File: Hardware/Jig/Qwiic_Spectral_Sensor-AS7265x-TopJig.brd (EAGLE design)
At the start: 35.6 x 40.6 mm, 93 parts, among them J2 Serial Interface, J5 Flash Programming, J8 PTH, U1 AS72651, U3 4MB Flash, U5 AS72653, U6 AS72652

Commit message: Silk changes before panelization
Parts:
- removed U$1, U$36, U$37: (no value), buzzard_labels (7):#0
- removed U$38, U$39, U$40: (no value), buzzard_labels (7):#1
- added E$1, E$2, E$3, E$4: (no value), SparkFun-Hardware:STAND-OFF-TIGHT
- added E$5, E$6: (no value), SparkFun-Hardware:NUBBIN_LOCKER
- D2: device SparkFun-LED:SUPER_BRIGHT_SMD_LED_3014 -> SparkX:SUPER_BRIGHT_SMD_LED_1206
- moved U$6 0.25 mm to (28.1, 21.3)
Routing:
- net 3.3V: track 143.3 -> 0.00 mm, vias 4 -> 0
- net RX/SCL: track 99.0 -> 0.00 mm, vias 6 -> 0
- net TX/SDA: track 93.2 -> 0.00 mm, vias 5 -> 0
- net SDA_S: track 56.9 -> 0.00 mm, vias 3 -> 0
- net SCL_S: track 56.2 -> 0.00 mm, vias 3 -> 0
- net !RST: track 50.8 -> 0.00 mm, vias 3 -> 0
- net !INT: track 30.2 -> 0.00 mm, vias 1 -> 0
- net LED_DRV: track 21.0 -> 0.00 mm, vias 1 -> 0
- net !CS_EE: track 17.6 -> 0.00 mm, vias 2 -> 0
- net I2C_ENB: track 16.8 -> 0.00 mm, vias 1 -> 0
- net MISO: track 15.5 -> 0.00 mm, vias 1 -> 0
- net !RST-ADDR: track 14.9 -> 0.00 mm, vias 2 -> 0
- net N$2: track 11.8 -> 0.00 mm, vias 2 -> 0
- net MOSI: track 9.65 -> 0.00 mm
- net LED_DRV1: track 9.51 -> 0.00 mm
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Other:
- board size 35.6 x 40.6 mm -> 48.3 x 53.3 mm
- board text added: "#6"
- board text added: "6"
- board text added: "DEV-Me"
- board text added: "GPS-Test"

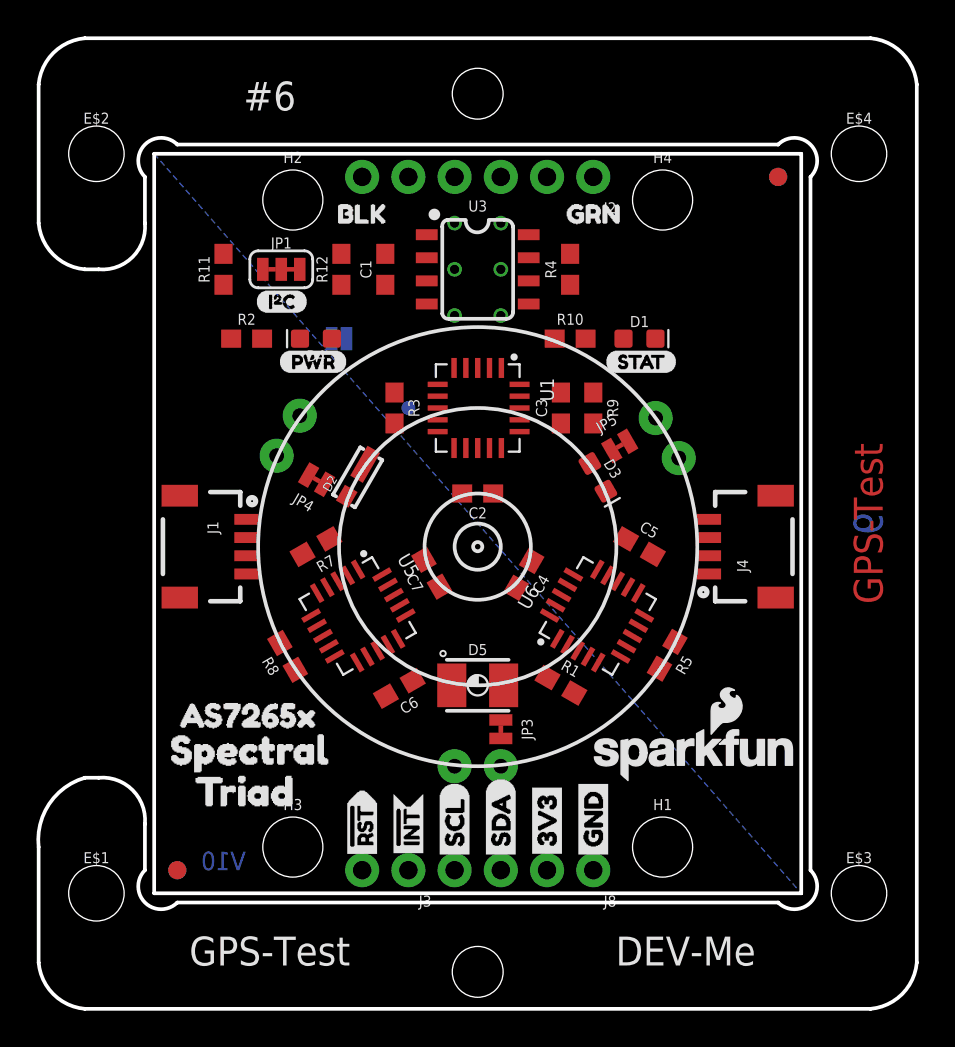
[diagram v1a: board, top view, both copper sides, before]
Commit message: Intermediate committ. Probably ignore the jig files.
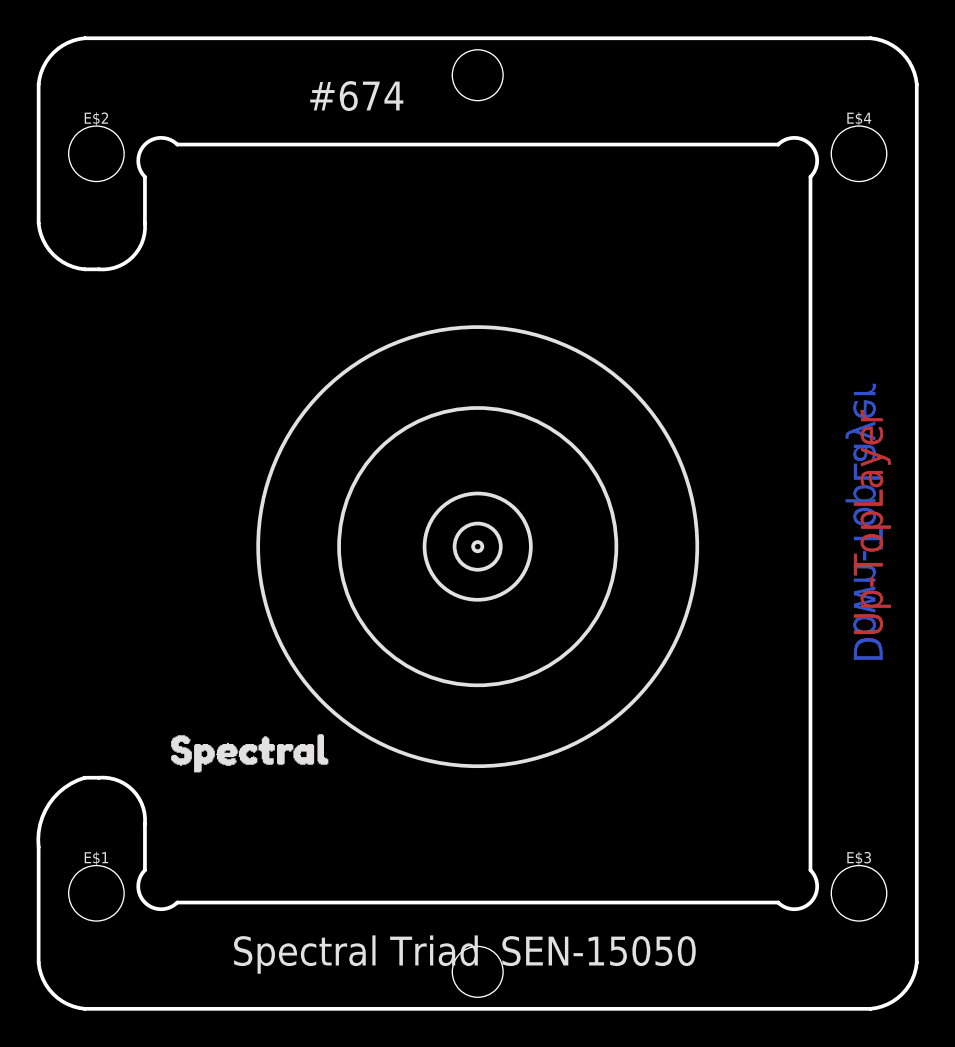
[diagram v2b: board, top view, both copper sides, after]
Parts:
- removed BULB1, BULB2, BULB3: (no value), SparkX:LED_5MM_NOSILK
- removed C1: 1.0uF, SparkFun-Capacitors:0603
- removed C2, C4, C6: 0.1uF, SparkFun-Capacitors:0603
- removed C3, C5, C7: 10uF, SparkFun-Capacitors:0603
- removed D1: BLUE, SparkFun-LED:LED-0603
- removed D2: 5700k, SparkX:SUPER_BRIGHT_SMD_LED_1206
- removed D3: IR, SparkFun-LED:LED-0603
- removed D4: RED, SparkFun-LED:LED-0603
- removed D5: UV, SparkFun-LED:PLCC-2
- removed FD1, FD2, FD3, FD4: FIDUCIAL1X2, SparkFun-Aesthetics:FIDUCIAL-1X2
- removed H1, H2, H3, H4: STAND-OFF, SparkFun-Hardware:STAND-OFF
- removed J1, J4: (no value), SparkFun-Connectors:1X04_1MM_RA
- removed J2: Serial Interface, SparkFun-Connectors:1X06_NO_SILK
- removed J3: (no value), SparkFun-Connectors:1X02_NO_SILK
- removed J5: Flash Programming, SparkFun-Connectors:2X3_TEST_POINTS
- removed J8: PTH, SparkFun-Connectors:1X04_NO_SILK
- removed JP1: (no value), SparkFun-Jumpers:SMT-JUMPER_3_2-NC_TRACE_SILK
- removed JP2: (no value), SparkFun-Jumpers:SMT-JUMPER_2_NO_SILK
- removed JP3, JP4, JP5: (no value), SparkFun-Jumpers:SMT-JUMPER_2_NC_TRACE_NO-SILK
- removed LOGO1: SFE_LOGO_NAME_FLAME.1_INCH, SparkFun-Aesthetics:SFE_LOGO_NAME_FLAME_.1
- removed LOGO4: OSHW-LOGOS, SparkFun-Aesthetics:OSHW-LOGO-S
- removed R1, R3, R4, R5, R7, R8: 10k, SparkFun-Resistors:0603
- removed R10, R11, R12, R9: 2.2k, SparkFun-Resistors:0603
- removed R2: 1k, SparkFun-Resistors:0603
- removed TP1: (no value), SparkFun-Connectors:PAD.03X.03
- removed U$10: (no value), buzzard_labels (50):STAT4
- removed U$11, U$12: (no value), buzzard_labels (50):TRIAD2
- removed U$13: (no value), buzzard_labels (50):SPECTRAL1
- removed U$14, U$4: (no value), buzzard_labels (50):AS7265X0
- removed U$15: (no value), buzzard_labels (51):3V33
- removed U$16: (no value), buzzard_labels (51):BLK7
- removed U$17: (no value), buzzard_labels (51):GND5
- removed U$18: (no value), buzzard_labels (51):GRN6
- removed U$19, U$20: (no value), buzzard_labels (51):NC4
- removed U$2: (no value), Labels:I_SUPER2_C-()-03
- removed U$21: (no value), buzzard_labels (51):RXI2
- removed U$22: (no value), buzzard_labels (51):SERIAL0
- removed U$23: (no value), buzzard_labels (51):TXO1
- removed U$24, U$31: (no value), Labels:3V3-04
- removed U$25, U$30: (no value), Labels:GND-04
- removed U$26, U$32: (no value), Labels:SDA-[)
- removed U$27, U$33: (no value), Labels:SCL-[)
- removed U$28, U$34: (no value), Labels:INT#-[<-04
- removed U$29, U$35: (no value), Labels:RST#-[>-04
- removed U$3: (no value), Labels:PWR-()-03
- removed U$5: (no value), buzzard_labels (50):BULB15
- removed U$6: (no value), buzzard_labels (50):BULB26
- removed U$7: (no value), buzzard_labels (50):BULB37
- removed U$8: (no value), buzzard_labels (52):JP20
- removed U1: AS72651, Qwiic_Spectral_Sensor-AS7265x:LGA20
- removed U3: 4MB Flash, SparkFun-IC-Memory:SO08
- removed U5: AS72653, Qwiic_Spectral_Sensor-AS7265x:LGA20
- removed U6: AS72652, Qwiic_Spectral_Sensor-AS7265x:LGA20
- moved E$6 1.02 mm to (17.8, 45.0)
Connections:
- removed net !CS_EE: J5.5, U1.6, U3.1
- removed net !INT: J3.1, U1.9
- removed net !RST: J3.2, R4.1, U1.2, U5.2
- removed net !RST-ADDR: U1.13, U6.2
- removed net 3.3V: BULB1.A, BULB2.A, BULB3.A, C1.1, C2.1, C3.1, C4.1, C5.1, C6.1, C7.1, D1.A, D4.A, J1.2, J2.4, J4.2, J5.2, J8.2, JP1.2, JP3.2, JP4.2, JP5.2, R10.2, R3.2, R4.2, R9.2, U1.14, U1.17, U3.3, U3.7, U3.8, U5.14, U5.17, U6.14, U6.17
- removed net GND: C1.2, C2.2, C3.2, C4.2, C5.2, C6.2, C7.2, J1.1, J2.6, J4.1, J5.6, J8.1, JP2.1, R1.1, R2.1, R5.1, R7.1, R8.1, U1.16, U3.4, U5.16, U6.16
- removed net I2C_ENB: JP2.2, R3.1, TP1.P$1, U1.8
- removed net LED_DRV: BULB1.K, D2.C, U1.15
- removed net LED_DRV1: BULB2.K, D3.C, U6.15
- removed net LED_DRV2: BULB3.K, D5.C, U5.15
- removed net MISO: J5.1, U1.5, U3.2
- removed net MOSI: J5.4, U1.4, U3.5
- removed net N$1: D4.C, R2.2
- removed net N$11: D5.A, JP3.1
- removed net N$12: R8.2, U5.7
- removed net N$13: R7.2, U5.5
- removed net N$2: D1.C, U1.18
- removed net N$3: R5.2, U6.7
- removed net N$4: JP1.3, R12.2
- removed net N$5: JP1.1, R11.2
- removed net N$6: D2.A, JP4.1
- removed net N$8: D3.A, JP5.1
- removed net N$9: R1.2, U6.5
- removed net RX/SCL: J1.4, J2.3, J4.4, J8.4, R11.1, U1.11
- removed net SCK: J5.3, U1.3, U3.6
- removed net SCL_S: R9.1, U1.20, U5.9, U6.9
- removed net SDA_S: R10.1, U1.1, U5.10, U6.10
- removed net TX/SDA: J1.3, J2.2, J4.3, J8.3, R12.1, U1.12
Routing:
- removed copper zone on layer 1, net GND
- removed copper zone on layer 16, net GND
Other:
- outline, holes or cut-outs redrawn
- board text added: "#674"
- board text added: "Down-TopLayer"
- board text added: "SEN-15050"
- board text added: "Spectral Triad"
- board text added: "Up-TopLayer"
- board text removed: "#6"
- board text removed: "6"
- board text removed: "DEV-Me"
- board text removed: "GPS-Test"
- board text removed: "V10"
